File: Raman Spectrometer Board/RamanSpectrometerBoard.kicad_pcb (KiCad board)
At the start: 2 copper layers, 104.8 x 62.1 mm, 60 parts, among them J1 1722861102, J2 Conn_01x02, J3 RJ45_LED_Shielded, J4 1722861102, J5 1722861102, Q1 AO3401A, Q2 BSS138, Q3 BSS138, Q4 AO3401A, Q5 BSS138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

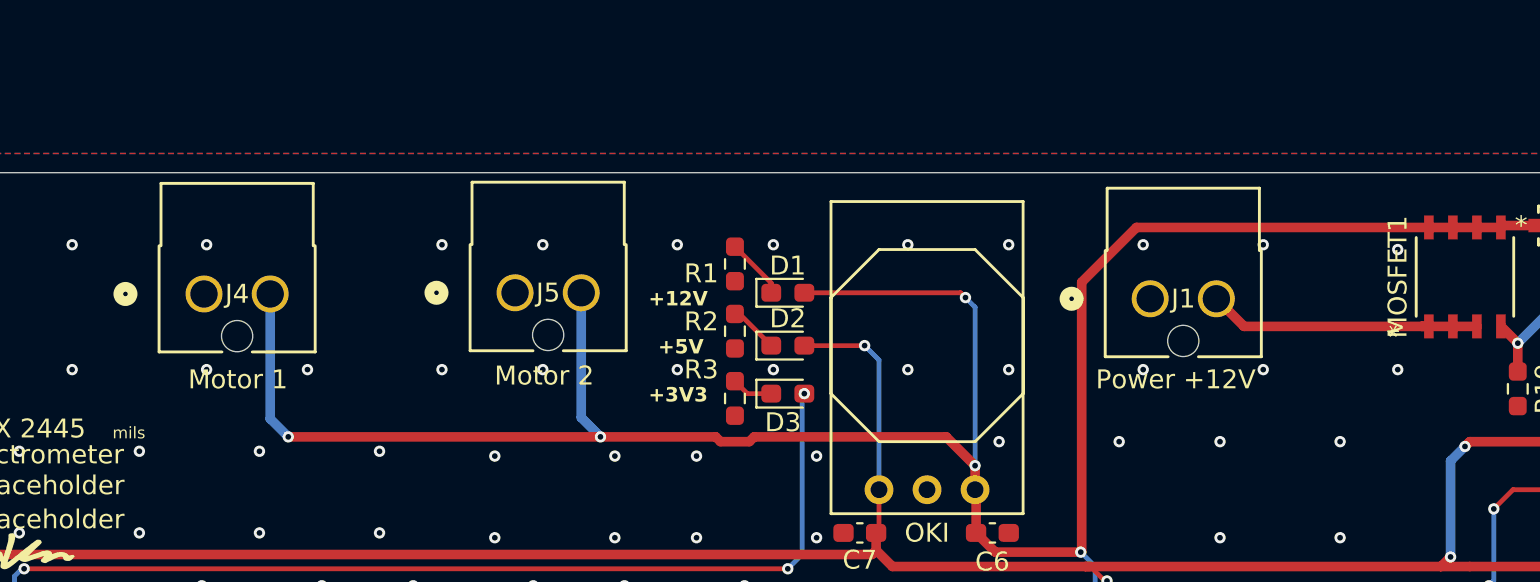
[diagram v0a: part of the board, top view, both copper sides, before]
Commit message: New Power Connectors
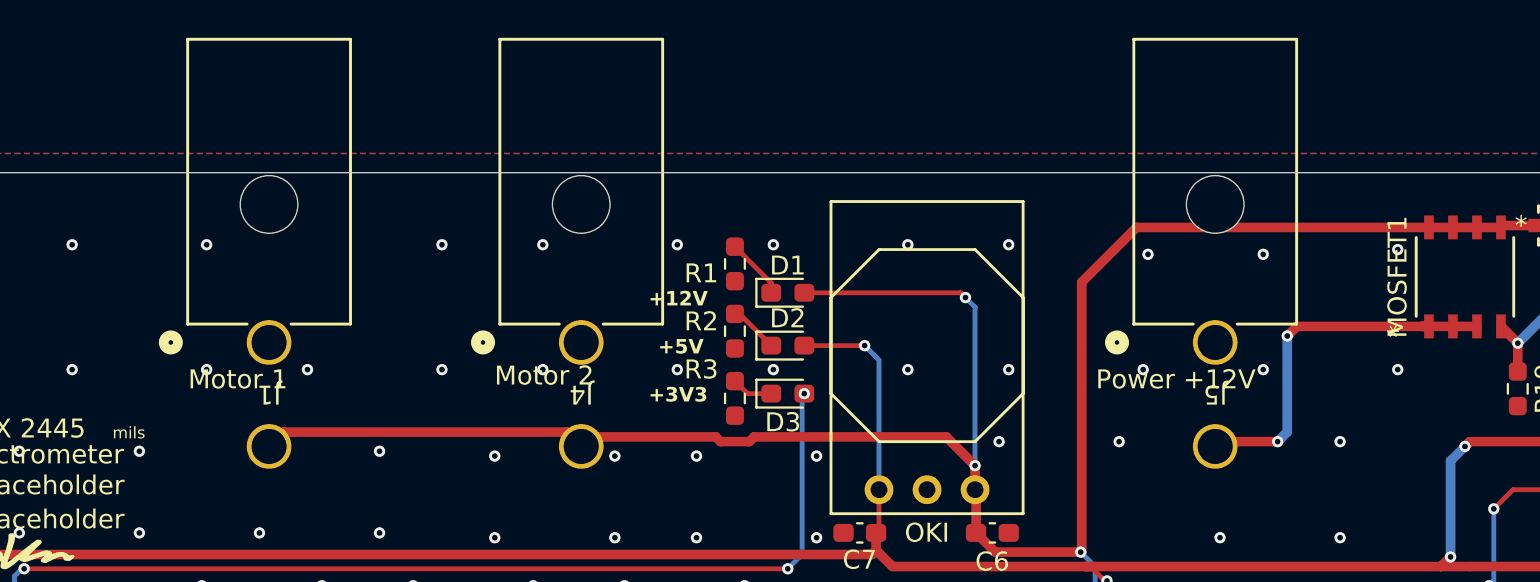
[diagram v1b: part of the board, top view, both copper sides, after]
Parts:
- J1, J4, J5: value 1722861102 -> 768250002; footprint MRDT_Connectors:CONN_SD-172286-1000_02_MOL -> Raman:CONN_SD-76825-0100_02_MOL
- moved J1 46.7 mm to (173.5, 58.3), turned to 180 degrees
- moved J5 37.1 mm to (223.5, 58.3), turned to 180 degrees
- moved J4 20.1 mm to (190.0, 58.3), turned to 180 degrees
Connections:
- J1 pad 2: Net-(J1-Pad2) -> +12V
- J5 pad 2: +12V -> Net-(J5-Pad2)
- MOSFET1 pad 1: Net-(J1-Pad2) -> Net-(J5-Pad2)
- MOSFET1 pad 2: Net-(J1-Pad2) -> Net-(J5-Pad2)
- MOSFET1 pad 3: Net-(J1-Pad2) -> Net-(J5-Pad2)
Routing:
- net Net-(J5-Pad2): track 0.00 -> 19.8 mm, vias 0 -> 2
- net Net-(J1-Pad2): track 14.8 -> 0.00 mm
- net +12V: track 164.1 -> 150.0 mm, vias 8 -> 7
- net GND: vias 154 -> 152

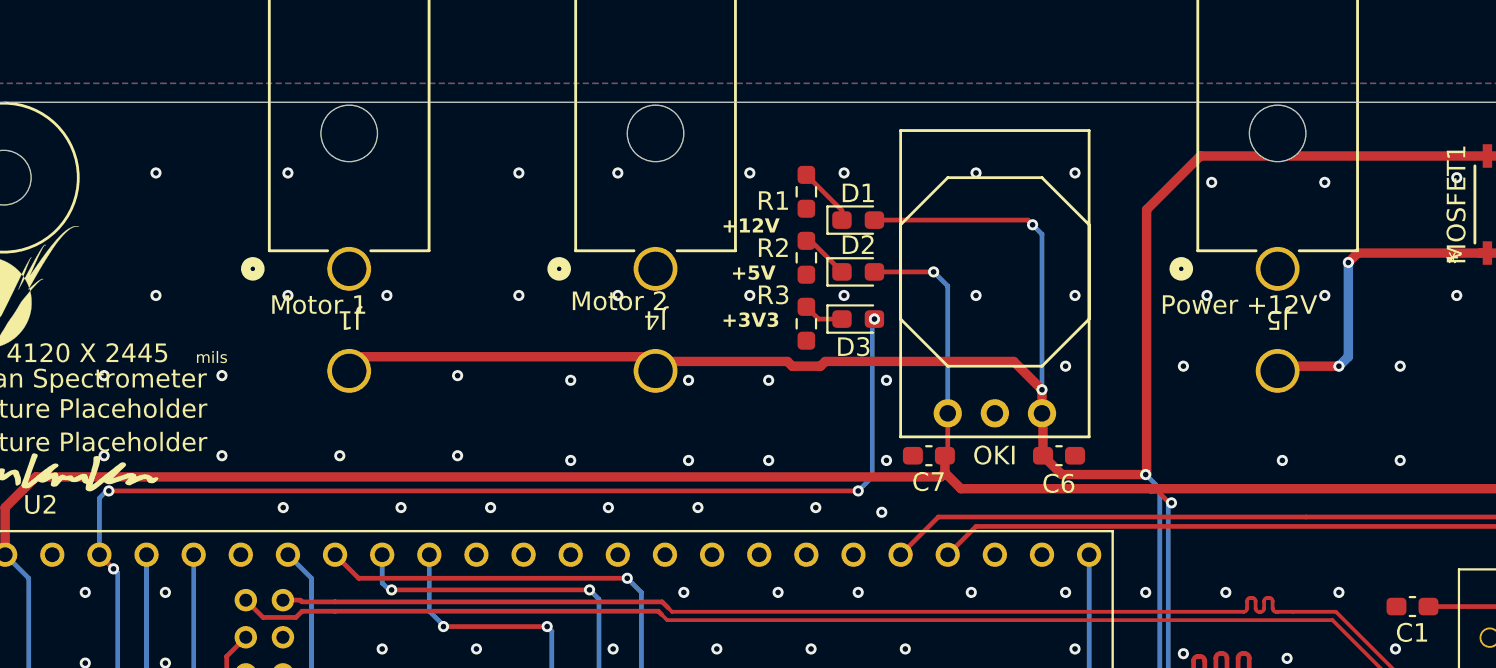
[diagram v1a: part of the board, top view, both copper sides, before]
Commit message: Add Motor Buttons
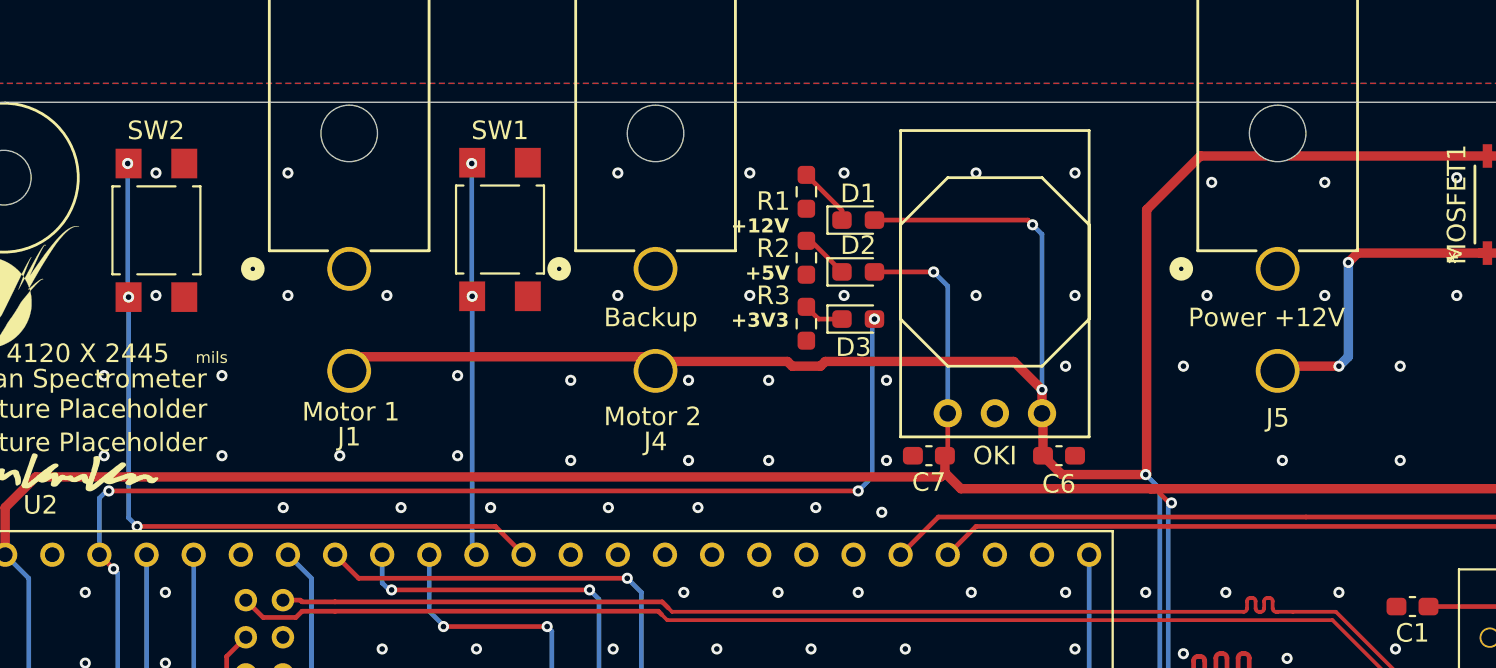
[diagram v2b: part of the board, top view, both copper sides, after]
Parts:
- added SW1: SW_Push, Button_Switch_SMD:SW_SPST_TL3305A, F.Cu at (181.6, 56.1)
- added SW2: SW_Push, Button_Switch_SMD:SW_SPST_TL3305A, F.Cu at (163.1, 56.2)
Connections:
- U2 pad 15: unconnected-(U2-A1-Pad15) -> /CAN Transceiver/SW1
- U2 pad 16: unconnected-(U2-A2-Pad16) -> /CAN Transceiver/SW2_Spare
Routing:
- net /CAN Transceiver/SW1: track 0.00 -> 41.3 mm, vias 0 -> 3
- net /CAN Transceiver/SW2_Spare: track 0.00 -> 21.2 mm, vias 0 -> 2
- net GND: vias 152 -> 150
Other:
- board text added: "Backup"
- board text added: "J1"

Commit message: Fix CDR
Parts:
- added Conn4: Molex_SL_02, MRDT_Connectors:MOLEX_SL_02_Vertical, F.Cu at (163.2, 65.6)
- added Conn6: Molex_SL_02, MRDT_Connectors:MOLEX_SL_02_Vertical, F.Cu at (154.5, 65.6)
- G*** (x2): moved to B.Cu
- moved G*** 9.78 mm to (164.1, 55.7), turned to 180 degrees
- moved G*** 4.64 mm to (159.7, 65.5)
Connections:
- U2 pad 7: unconnected-(U2-RX2-Pad7) -> /Connectors/LSwitch1
- U2 pad 8: unconnected-(U2-TX2-Pad8) -> /Connectors/LSwitch2
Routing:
- net /Connectors/LSwitch1: track 0.00 -> 59.3 mm, vias 0 -> 4
- net /Connectors/LSwitch2: track 0.00 -> 53.5 mm, vias 0 -> 4
- net +3V3: track 230.0 -> 244.8 mm, vias 17 -> 20
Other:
- board text added: "Sample Servo 1"
- board text added: "Spare Servo 2"
- board text removed: "Servo 1"
- board text removed: "Servo 2"

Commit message: labeling
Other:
- board text added: "CANH"
- board text added: "CANL"
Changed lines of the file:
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@@
 		(layer "Edge.Cuts")
+	)
+	(gr_text "CANL"
+		(at 161.5 110.5 0)
+		(layer "F.SilkS")
+		(effects
+			(font
+				(size 0.5 0.5)
+				(thickness 0.125)
+				(bold yes)
+			)
+			(justify left bottom)
+		)
 	)
 	(gr_text "J1"
@@
 				(size 1 1)
 				(thickness 0.1508)
+			)
+			(justify left bottom)
+		)
+	)
+	(gr_text "CANH"
+		(at 164 110.5 0)
+		(layer "F.SilkS")
+		(effects
+			(font
+				(size 0.5 0.5)
+				(thickness 0.125)
+				(bold yes)
 			)
 			(justify left bottom)
@@
 			(keep_text_aligned yes)
 		)
-		(gr_text "2445"
+		(gr_text "62.103"
 			(at 268.5726 80.3275 90)
 			(layer "Dwgs.User")
@@
 			(keep_text_aligned yes)
 		)
-		(gr_text "2125"
+		(gr_text "53.975"
 			(at 264.788 80.322419 90)
 			(layer "Dwgs.User")
@@
 			(keep_text_aligned yes)
 		)
-		(gr_text "3800"
+		(gr_text "96.52"
 			(at 203.12266 30.092 0)
 			(layer "Dwgs.User")
@@
 			(keep_text_aligned yes)
 		)
-		(gr_text "4120"
+		(gr_text "104.648"
 			(at 203.2 37.458 0)
 			(layer "Dwgs.User")

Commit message: layout labelling
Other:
- board text added: "EOS"
- board text added: "GND"
- board text added: "GPID"
- board text added: "IN"
- board text added: "SCL"
- board text added: "SDA"
- board text added: "ST"
- board text added: "Servo2"
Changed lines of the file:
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@@
 		(layer "Edge.Cuts")
+	)
+	(gr_text "+5V"
+		(at 254.5 96 90)
+		(layer "F.SilkS")
+		(effects
+			(font
+				(size 0.5 0.5)
+				(thickness 0.125)
+				(bold yes)
+			)
+			(justify left bottom)
+		)
 	)
 	(gr_text "CANL"
@@
 		)
 	)
+	(gr_text "EOS"
+		(at 231.5 110.5 0)
+		(layer "F.SilkS")
+		(effects
+			(font
+				(size 0.5 0.5)
+				(thickness 0.125)
+				(bold yes)
+			)
+			(justify left bottom)
+		)
+	)
 	(gr_text "Backup"
 		(at 187.198 61.468 0)
@@
 		)
 	)
+	(gr_text "GPID"
+		(at 184 110.5 0)
+		(layer "F.SilkS")
+		(effects
+			(font
+				(size 0.5 0.5)
+				(thickness 0.125)
+				(bold yes)
+			)
+			(justify left bottom)
+		)
+	)
 	(gr_text "Sample Servo 1\n"
 		(at 248.3 71.9 90)
@@
 		)
 	)
+	(gr_text "CANL"
+		(at 172.5 110.5 0)
+		(layer "F.SilkS")
+		(effects
+			(font
+				(size 0.5 0.5)
+				(thickness 0.125)
+				(bold yes)
+			)
+			(justify left bottom)
+		)
+	)
+	(gr_text "+3V3"
+		(at 194 110.5 0)
+		(layer "F.SilkS")
+		(effects
+			(font
+				(size 0.5 0.5)
+				(thickness 0.125)
+				(bold yes)
+			)
+			(justify left bottom)
+		)
+	)
+	(gr_text "GND"
+		(at 216 110.5 0)
+		(layer "F.SilkS")
+		(effects
+			(font
+				(size 0.5 0.5)
+				(thickness 0.125)
+				(bold yes)
+			)
+			(justify left bottom)
+		)
+	)
+	(gr_text "Servo2"
+		(at 254.5 99 90)
+		(layer "F.SilkS")
+		(effects
+			(font
+				(size 0.5 0.5)
+				(thickness 0.125)
+				(bold yes)
+			)
+			(justify left bottom)
+		)
+	)
+	(gr_text "SCL"
+		(at 189.5 110.5 0)
+		(layer "F.SilkS")
+		(effects
+			(font
+				(size 0.5 0.5)
+				(thickness 0.125)
+				(bold yes)
+			)
+			(justify left bottom)
+		)
+	)
 	(gr_text "Motor 1"
 		(at 170.942 66.548 0)
@@
 				(size 1 1)
 				(thickness 0.15)
+			)
+			(justify left bottom)
+		)
+	)
+	(gr_text "CANH"
+		(at 175 110.5 0)
+		(layer "F.SilkS")
+		(effects
+			(font
+				(size 0.5 0.5)
+				(thickness 0.125)
+				(bold yes)
 			)
 			(justify left bottom)
@@
 		)
 	)
+	(gr_text "GND"
+		(at 224 110.5 0)
+		(layer "F.SilkS")
+		(effects
+			(font
+				(size 0.5 0.5)
+				(thickness 0.125)
+				(bold yes)
+			)
+			(justify left bottom)
+		)
+	)
+	(gr_text "ST"
+		(at 229 110.5 0)
+		(layer "F.SilkS")
+		(effects
+			(font
+				(size 0.5 0.5)
+				(thickness 0.125)
+				(bold yes)
+			)
+			(justify left bottom)
+		)
+	)
 	(gr_text "Power +12V\n"
 		(at 218.694 61.468 0)
@@
 		)
 	)
+	(gr_text "+5V"
+		(at 239 110.5 0)
+		(layer "F.SilkS")
+		(effects
+			(font
+				(size 0.5 0.5)
+				(thickness 0.125)
+				(bold yes)
+			)
+			(justify left bottom)
+		)
+	)
 	(gr_text "Fan"
 		(at 219.6 108.4 270)
@@
 		)
 	)
+	(gr_text "SDA"
+		(at 187 110.5 0)
+		(layer "F.SilkS")
+		(effects
+			(font
+				(size 0.5 0.5)
+				(thickness 0.125)
+				(bold yes)
+			)
+			(justify left bottom)
+		)
+	)
+	(gr_text "GND"
+		(at 254.5 101 90)
+		(layer "F.SilkS")
+		(effects
+			(font
+				(size 0.5 0.5)
+				(thickness 0.125)
+				(bold yes)
+			)
+			(justify left bottom)
+		)
+	)
 	(gr_text "Spare Servo 2"
 		(at 247.4 103.5 90)
@@
 				(size 1 1)
 				(thickness 0.15)
+			)
+			(justify left bottom)
+		)
+	)
+	(gr_text "IN"
+		(at 237 110.5 0)
+		(layer "F.SilkS")
+		(effects
+			(font
+				(size 0.5 0.5)
+				(thickness 0.125)
+				(bold yes)
 			)
 			(justify left bottom)
@@
 		)
 	)
+	(gr_text "GND"
+		(at 192 110.5 0)
+		(layer "F.SilkS")
+		(effects
+			(font
+				(size 0.5 0.5)
+				(thickness 0.125)
+				(bold yes)
+			)
+			(justify left bottom)
+		)
+	)
 	(gr_text "CAN 1"
 		(at 167.8 106.426 270)
@@
 		)
 	)
+	(gr_text "+3V3"
+		(at 181.5 110.5 0)
+		(layer "F.SilkS")
+		(effects
+			(font
+				(size 0.5 0.5)
+				(thickness 0.125)
+				(bold yes)
+			)
+			(justify left bottom)
+		)
+	)
 	(gr_text "TOF\n\n"
 		(at 196.4 108.2 270)
@@
 			)
 			(justify left bottom)
+		)
+	)
+	(gr_text "+3V3"
+		(at 241.5 110.5 0)
+		(layer "F.SilkS")
+		(effects
+			(font
+				(size 0.5 0.5)
+				(thickness 0.125)
+				(bold yes)
+			)
+			(justify left bottom)

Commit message: PCB final design? maybe
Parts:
- added G***: LOGO, Silkscreens:MST, F.Cu at (218.4, 72.1)
- added S1: SLW-913535-2A-SMT, Raman:SW_SLW-913535-2A-SMT, F.Cu at (191.3, 99.3)
- G*** (x2): moved to F.Cu
- moved G*** 69.3 mm to (226.6, 83.7), turned to 180 degrees
- moved G*** 62.4 mm to (224.5, 71.2), turned to 90 degrees
- moved J1 1.22 mm to (173.5, 59.5)
- moved J4 1.22 mm to (190.0, 59.5)
- moved J5 1.22 mm to (223.5, 59.5)
- moved C3 0.51 mm to (167.8, 98.3)
- moved R12 0.14 mm to (227.4, 96.4)
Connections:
- net /Connectors/LSwitch1 renamed /Connectors/D1
- net /Connectors/LSwitch2 renamed /Connectors/D2
- Conn1 pad 1: Net-(U3-CANH) -> Net-(Conn1-Pad1)
- Conn1 pad 2: Net-(U3-CANL) -> Net-(Conn1-Pad2)
- Conn2 pad 1: Net-(U1-CANH) -> Net-(Conn1-Pad1)
- Conn2 pad 2: Net-(U1-CANL) -> Net-(Conn1-Pad2)
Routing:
- net Net-(Conn1-Pad2): track 0.00 -> 52.5 mm, vias 0 -> 4
- net Net-(Conn1-Pad1): track 0.00 -> 38.5 mm, vias 0 -> 4
- net Net-(U3-CANL): track 13.0 -> 43.3 mm, vias 2 -> 4
- net Net-(U3-CANH): track 12.4 -> 31.0 mm, vias 3 -> 2
- net Net-(U1-CANL): track 11.7 -> 29.9 mm
- net Net-(U1-CANH): track 12.5 -> 22.4 mm
- net +12V: track 150.0 -> 152.7 mm, vias 7 -> 6
- net Net-(J5-Pad2): track 19.8 -> 21.1 mm
- net /CCD Breakout/ST: track 82.5 -> 83.6 mm
- net +3V3: track 244.8 -> 244.2 mm
- net GND: vias 150 -> 139
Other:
- board text added: "+V"
- board text added: "CLK1"
- board text added: "CLK2"
- board text added: "LIMSW1"
- board text added: "LIMSW2"
- board text added: "Servo1"

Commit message: signature
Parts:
- added G***: LOGO, LOGO, F.Cu at (224.5, 84.0)

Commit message: Signature
Added Signature
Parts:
- added G***: LOGO, LOGO, F.Cu at (222.9, 85.4)
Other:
- board text removed: "Signiture Placeholder"
